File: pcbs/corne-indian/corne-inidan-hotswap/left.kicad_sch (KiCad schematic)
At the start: 88 parts, among them J1 Conn_01x03_Pin, J2 Conn_01x04_Pin, J3 PJ-3136-B, SW1 SW_Push, SW10 SW_Push, SW11 SW_Push, SW12 SW_Push, SW13 SW_Push, SW14 SW_Push, SW15 SW_Push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

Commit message: PCB Layout is almost done Cosmetic Chnages need to do
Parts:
- EXSW1, EXSW2: footprint User_Button_Switch_Keyboard:keyswitch_cherrymx_hotswap_1u_rotary_encoder_ec12 -> User_Button_Switch_Keyboard:SW_Cherry_MX_1.00u_Hotswap_Rotary-Encoder
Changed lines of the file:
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@@
 			)
 		)
-		(property "Footprint" "User_Button_Switch_Keyboard:keyswitch_cherrymx_hotswap_1u_rotary_encoder_ec12"
+		(property "Footprint" "User_Button_Switch_Keyboard:SW_Cherry_MX_1.00u_Hotswap_Rotary-Encoder"
 			(at 264.414 129.54 0)
 			(effects
@@
 			)
 		)
-		(property "Footprint" "User_Button_Switch_Keyboard:keyswitch_cherrymx_hotswap_1u_rotary_encoder_ec12"
+		(property "Footprint" "User_Button_Switch_Keyboard:SW_Cherry_MX_1.00u_Hotswap_Rotary-Encoder"
 			(at 264.414 180.34 0)
 			(effects

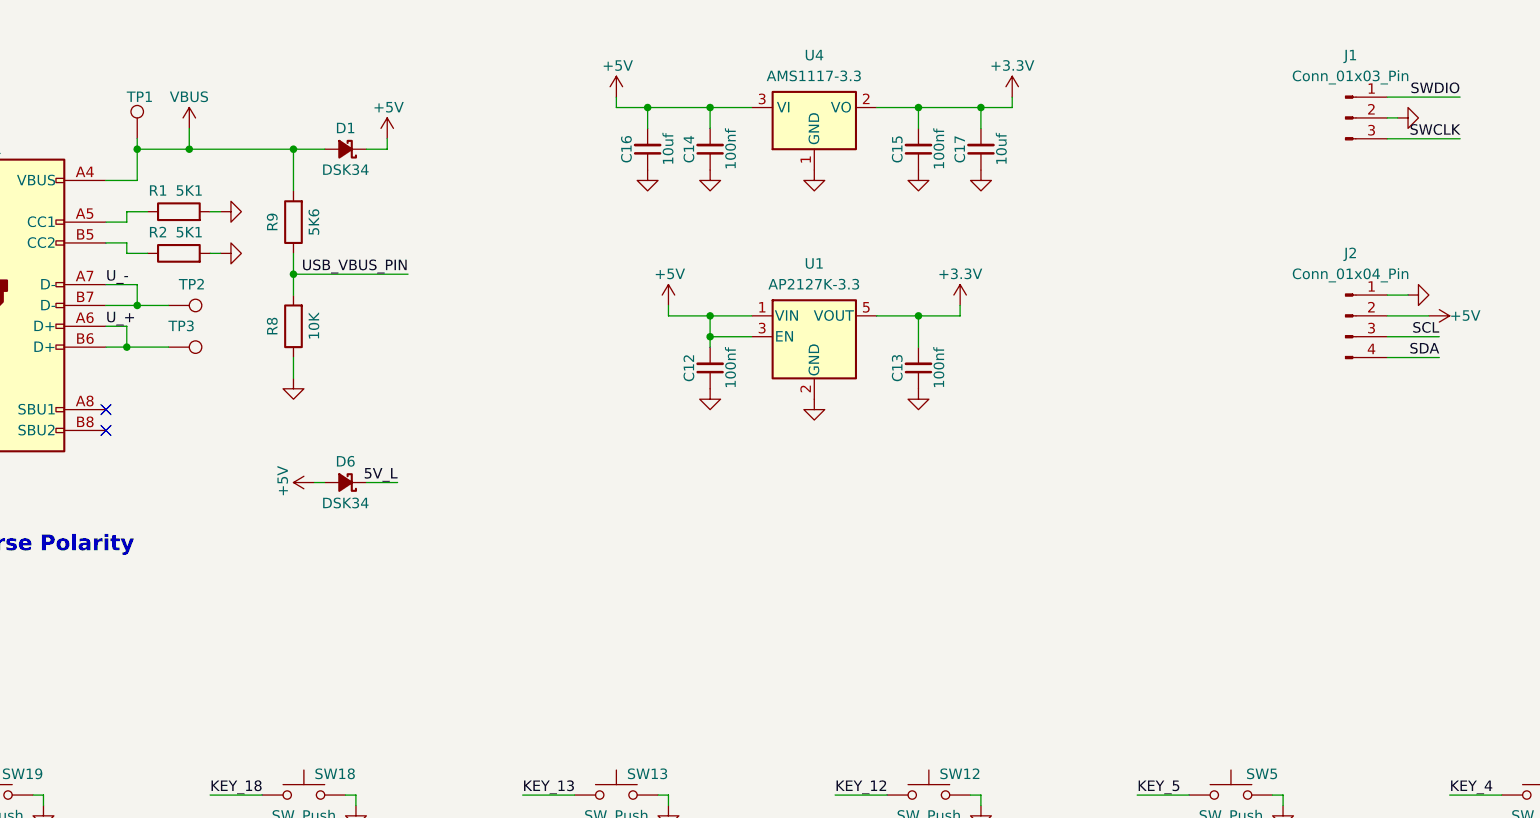
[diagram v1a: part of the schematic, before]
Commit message: USB Circuit deleted & Design is also compeleted in LAyout level
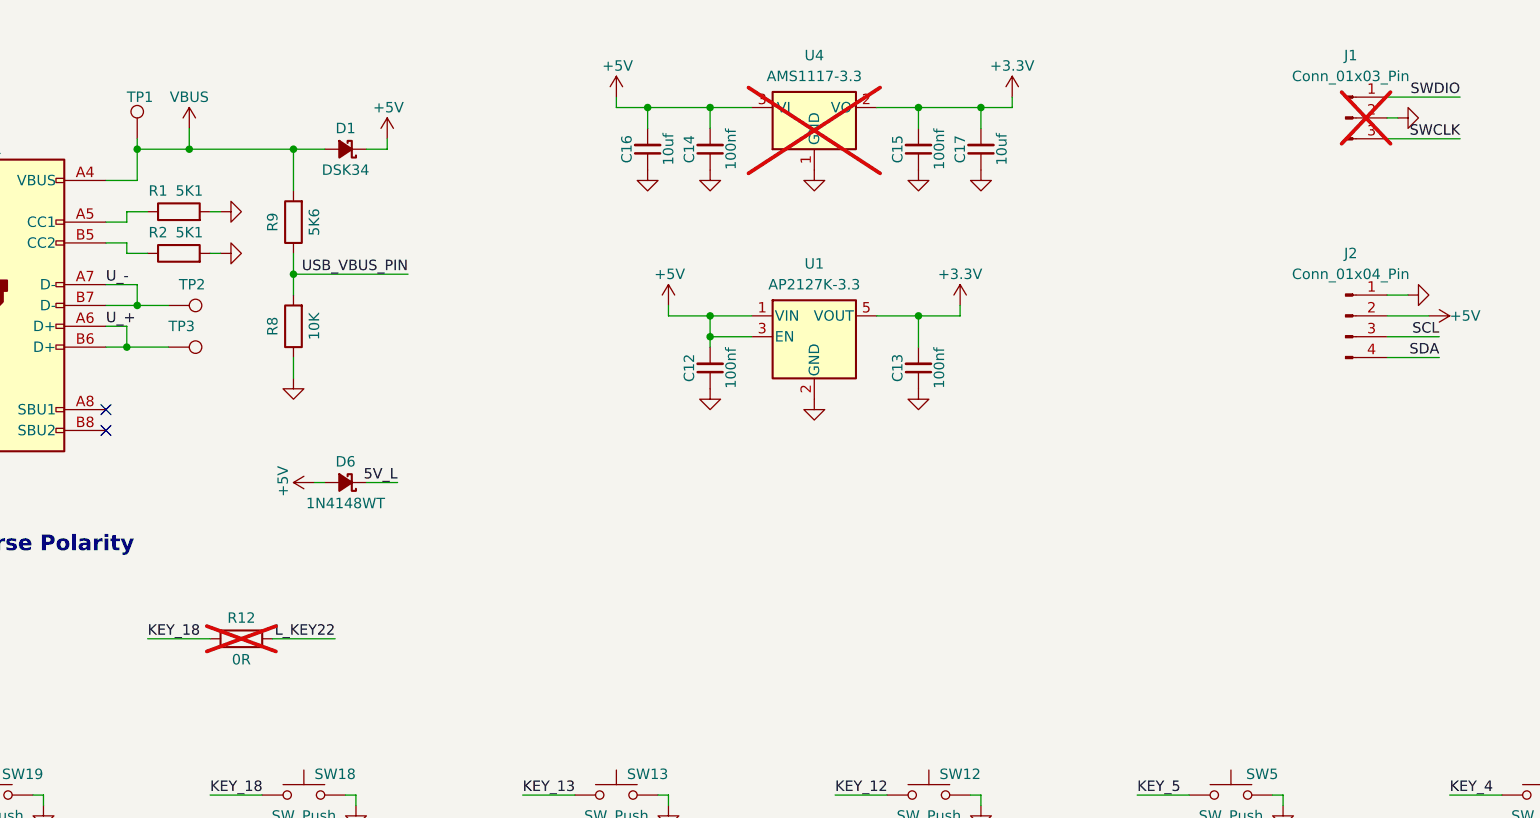
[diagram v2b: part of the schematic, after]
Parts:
- added R12: 0R, Resistor_SMD:R_0603_1608Metric, symbol Device:R
- D6: value DSK34 -> 1N4148WT
- J1, U4: now not fitted; now left out of the parts list
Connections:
- net KEY_18: now also R12.2
- net L_KEY22: now also R12.1
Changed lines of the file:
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@@
 	(wire
 		(pts
+			(xy 58.42 95.25) (xy 66.04 95.25)
+		)
+		(stroke
+			(width 0)
+			(type default)
+		)
+	)
+	(wire
+		(pts
 			(xy 27.94 190.5) (xy 34.29 190.5)
 		)
@@
 	(wire
 		(pts
+			(xy 73.66 95.25) (xy 81.28 95.25)
+		)
+		(stroke
+			(width 0)
+			(type default)
+		)
+	)
+	(wire
+		(pts
 			(xy 257.81 120.65) (xy 257.81 125.73)
 		)
@@
 		)
 	)
+	(label "KEY_18"
+		(at 58.42 95.25 0)
+		(effects
+			(font
+				(size 1.27 1.27)
+			)
+			(justify left bottom)
+		)
+	)
 	(label "L_KEY13"
 		(at 101.6 127 0)
@@
 		)
 	)
+	(label "L_KEY22"
+		(at 81.28 95.25 180)
+		(effects
+			(font
+				(size 1.27 1.27)
+			)
+			(justify right bottom)
+		)
+	)
 	(label "L_KEY4"
 		(at 215.9 127 0)
@@
 		(unit 1)
 		(exclude_from_sim no)
-		(in_bom yes)
+		(in_bom no)
 		(on_board yes)
-		(dnp no)
+		(dnp yes)
 		(fields_autoplaced yes)
 		(property "Reference" "U4"
@@
 			)
 		)
-		(property "Value" "DSK34"
+		(property "Value" "1N4148WT"
 			(at 82.55 78.74 0)
 			(effects
@@
 		(unit 1)
 		(exclude_from_sim no)
-		(in_bom yes)
+		(in_bom no)
 		(on_board yes)
-		(dnp no)
+		(dnp yes)
 		(fields_autoplaced yes)
 		(property "Reference" "J1"
@@
 					(unit 1)
 				)
+			)
+		)
+	)
+	(symbol
+		(lib_id "Device:R")
+		(at 69.85 95.25 270)
+		(mirror x)
+		(unit 1)
+		(exclude_from_sim no)
+		(in_bom no)
+		(on_board yes)
+		(dnp yes)
+		(property "Reference" "R12"
+			(at 69.85 92.71 90)
+			(effects
+				(font
+					(size 1.27 1.27)
+				)
+			)
+		)
+		(property "Value" "0R"
+			(at 69.85 97.79 90)
+			(effects
+				(font
+					(size 1.27 1.27)
+				)
+			)
+		)
+		(property "Footprint" "Resistor_SMD:R_0603_1608Metric"
+			(at 69.85 97.028 90)
+			(effects
+				(font
+					(size 1.27 1.27)
+				)
+				(hide yes)
+			)
+		)
+		(property "Datasheet" "~"
+			(at 69.85 95.25 0)
+			(effects
+				(font
+					(size 1.27 1.27)
+				)
+				(hide yes)
+			)
+		)
+		(property "Description" "Resistor"
+			(at 69.85 95.25 0)
+			(effects
+				(font
+					(size 1.27 1.27)
+				)
+				(hide yes)
+			)
+		)
+		(property "LCSC_Part" "C25804"
+			(at 69.85 95.25 90)
+			(effects
+				(font
+					(size 1.27 1.27)
+				)
+				(hide yes)
+			)
+		)
+		(property "Manufacturer_Name" "MULTICOMP PRO"
+			(at 69.85 95.25 90)
+			(effects
+				(font
+					(size 1.27 1.27)
+				)
+				(hide yes)
+			)
+		)
+		(property "Manufacturer_Name_1" ""
+			(at 69.85 95.25 90)
+			(effects
+				(font
+					(size 1.27 1.27)
+				)
+				(hide yes)
+			)
+		)
+		(property "Manufacturer_Name_2" "UNI-ROYAL(Uniroyal Elec)"
+			(at 69.85 95.25 90)
+			(effects
+				(font
+					(size 1.27 1.27)
+				)
+				(hide yes)
+			)
+		)
+		(property "Manufacturer_Part_Number" "MCWR06X1002FTL"
+			(at 69.85 95.25 90)
+			(effects
+				(font
+					(size 1.27 1.27)
+				)
+				(hide yes)
+			)
+		)
+		(property "Manufacturer_Part_Number_1" ""
+			(at 69.85 95.25 90)
+			(effects
+				(font
+					(size 1.27 1.27)
+				)
+				(hide yes)
+			)
+		)
+		(property "Manufacturer_Part_Number_2" "0603WAF1002T5E"
+			(at 69.85 95.25 90)
+			(effects
+				(font
+					(size 1.27 1.27)
+				)
+				(hide yes)
+			)
+		)
+		(pin "1"
+		)
+		(pin "2"
+		)
+		(instances
+			(project "corne-inidan-hotswap"
+				(path "/c90c0725-f1d3-4c5d-9757-c1f2f2a5449f/f4940f7d-bc6d-4495-a44d-e8b9a3eadf42"
+					(reference "R12")
+					(unit 1)
+				)
